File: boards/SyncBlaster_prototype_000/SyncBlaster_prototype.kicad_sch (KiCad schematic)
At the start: 19 parts, among them J1 DIN-5 MIDI IN, J2 TRS SYNC IN START/STOP, U1 4066, U2 ATtiny25-20P, U3 CNY17-3

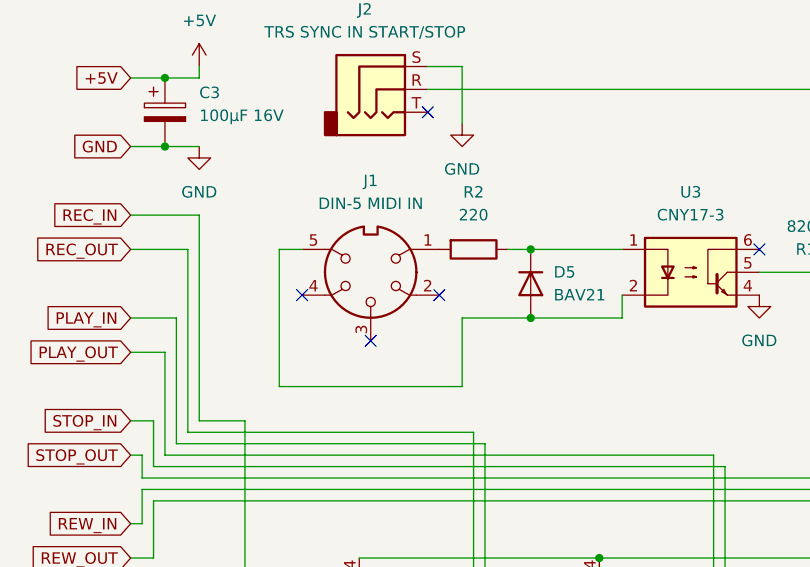
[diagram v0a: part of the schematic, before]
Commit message: prototype_000 board schematics release 3, MIDI OUT connection fix
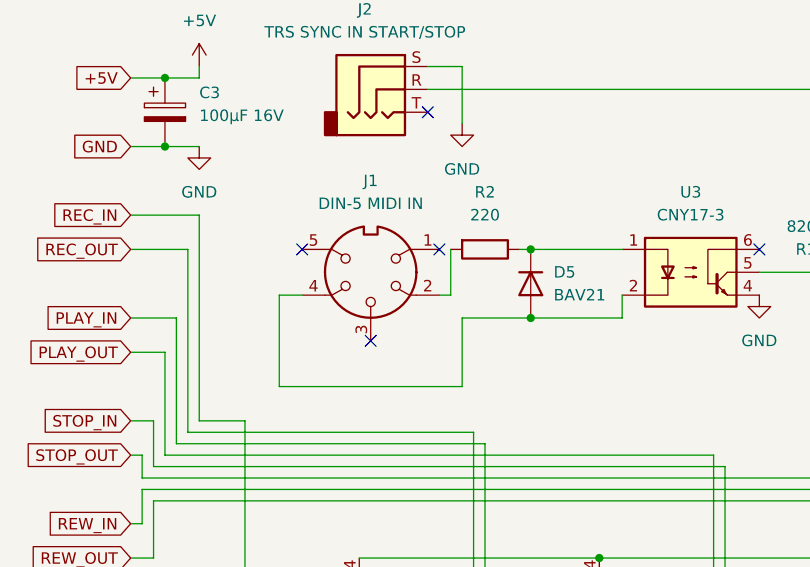
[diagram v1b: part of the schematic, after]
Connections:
- net at R2.2: now also J1.2; no longer J1.1
- net at J1.4: now also D5.2 (A), U3.2
- now unconnected: J1.5
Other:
- company: Copyright (c) Mateusz Maciejewski ^ TOXIC_DEATH.117, 2021 - 2023 -> Copyright (c) Mateusz Maciejewski ^ TOXIC_DEATH.117, 2021 - 2024
- moved on the sheet: R2
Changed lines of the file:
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@@
   (title_block
     (title "MIDI input interface for TASCAM DP00x")
-    (date "2023-06-16")
-    (rev "2")
-    (company "Copyright (c) Mateusz Maciejewski ^ TOXIC_DEATH.117, 2021 - 2023")
+    (date "2024-04-04")
+    (rev "3")
+    (company "Copyright (c) Mateusz Maciejewski ^ TOXIC_DEATH.117, 2021 - 2024")
   )
   (junction (at 93.98 107.95) (diameter 0) (color 0 0 0 0)
@@
   )
   (no_connect (at 119.38 107.95))
+  (no_connect (at 68.58 107.95))
   (no_connect (at 82.55 92.71))
-  (no_connect (at 68.58 113.03))
-  (no_connect (at 83.82 113.03))
+  (no_connect (at 83.82 107.95))
   (no_connect (at 76.2 118.11))
   (wire (pts (xy 176.53 157.48) (xy 154.94 157.48))
@@
     (stroke (width 0) (type default))
   )
-  (wire (pts (xy 66.04 107.95) (xy 68.58 107.95))
-    (stroke (width 0) (type default))
-  )
   (wire (pts (xy 49.53 115.57) (xy 54.61 115.57))
     (stroke (width 0) (type default))
@@
     (stroke (width 0) (type default))
   )
+  (wire (pts (xy 85.09 113.03) (xy 85.09 107.95))
+    (stroke (width 0) (type default))
+  )
   (wire (pts (xy 115.57 166.37) (xy 170.18 166.37))
     (stroke (width 0) (type default))
@@
     (stroke (width 0) (type default))
   )
+  (wire (pts (xy 66.04 113.03) (xy 68.58 113.03))
+    (stroke (width 0) (type default))
+  )
   (wire (pts (xy 134.62 110.49) (xy 134.62 91.44))
     (stroke (width 0) (type default))
@@
     (stroke (width 0) (type default))
   )
-  (wire (pts (xy 66.04 107.95) (xy 66.04 123.19))
+  (wire (pts (xy 66.04 113.03) (xy 66.04 123.19))
     (stroke (width 0) (type default))
   )
@@
     (stroke (width 0) (type default))
   )
-  (wire (pts (xy 91.44 107.95) (xy 93.98 107.95))
+  (wire (pts (xy 92.71 107.95) (xy 93.98 107.95))
     (stroke (width 0) (type default))
   )
@@
   )
   (wire (pts (xy 172.72 163.83) (xy 172.72 109.22))
+    (stroke (width 0) (type default))
+  )
+  (wire (pts (xy 85.09 113.03) (xy 83.82 113.03))
     (stroke (width 0) (type default))
   )
@@
     )
   )
-  (symbol (lib_id "Device:R") (at 87.63 107.95 270) (unit 1)
+  (symbol (lib_id "Device:R") (at 88.9 107.95 270) (unit 1)
     (in_bom yes) (on_board yes) (dnp no)
-    (property "Reference" "R2" (at 87.63 101.6 90)
-      (effects (font (size 1.27 1.27)))
-    )
-    (property "Value" "220" (at 87.63 104.14 90)
-      (effects (font (size 1.27 1.27)))
-    )
-    (property "Footprint" "" (at 87.63 106.172 90)
-      (effects (font (size 1.27 1.27)) hide)
-    )
-    (property "Datasheet" "~" (at 87.63 107.95 0)
-      (effects (font (size 1.27 1.27)) hide)
-    )
-    (pin "1")
-    (pin "2")
-    (instances
-      (project "SyncBlaster"
+    (property "Reference" "R2" (at 88.9 101.6 90)
+      (effects (font (size 1.27 1.27)))
+    )
+    (property "Value" "220" (at 88.9 104.14 90)
+      (effects (font (size 1.27 1.27)))
+    )
+    (property "Footprint" "" (at 88.9 106.172 90)
+      (effects (font (size 1.27 1.27)) hide)
+    )
+    (property "Datasheet" "~" (at 88.9 107.95 0)
+      (effects (font (size 1.27 1.27)) hide)
+    )
+    (pin "1")
+    (pin "2")
+    (instances
+      (project "SyncBlaster_prototype"
         (path "/32dfbc9d-88bc-4ac5-b7ea-f4ca99c6c011"
           (reference "R2") (unit 1)
@@
     (pin "5")
     (instances
-      (project "SyncBlaster"
+      (project "SyncBlaster_prototype"
         (path "/32dfbc9d-88bc-4ac5-b7ea-f4ca99c6c011"
           (reference "J1") (unit 1)
@@
     (pin "T")
     (instances
-      (project "SyncBlaster"
+      (project "SyncBlaster_prototype"
         (path "/32dfbc9d-88bc-4ac5-b7ea-f4ca99c6c011"
           (reference "J2") (unit 1)
@@
     (pin "12")
     (instances
-      (project "SyncBlaster"
+      (project "SyncBlaster_prototype"
         (path "/32dfbc9d-88bc-4ac5-b7ea-f4ca99c6c011"
           (reference "U1") (unit 2)
@@
     (pin "1")
     (instances
-      (project "SyncBlaster"
+      (project "SyncBlaster_prototype"
         (path "/32dfbc9d-88bc-4ac5-b7ea-f4ca99c6c011"
           (reference "#PWR06") (unit 1)
@@
     (pin "1")
     (instances
-      (project "SyncBlaster"
+      (project "SyncBlaster_prototype"
         (path "/32dfbc9d-88bc-4ac5-b7ea-f4ca99c6c011"
           (reference "#PWR010") (unit 1)
@@
     (pin "1")
     (instances
-      (project "SyncBlaster"
+      (project "SyncBlaster_prototype"
         (path "/32dfbc9d-88bc-4ac5-b7ea-f4ca99c6c011"
           (reference "#PWR09") (unit 1)
@@
     (pin "2")
     (instances
-      (project "SyncBlaster"
+      (project "SyncBlaster_prototype"
         (path "/32dfbc9d-88bc-4ac5-b7ea-f4ca99c6c011"
           (reference "D3") (unit 1)
@@
     (pin "2")
     (instances
-      (project "SyncBlaster"
+      (project "SyncBlaster_prototype"
         (path "/32dfbc9d-88bc-4ac5-b7ea-f4ca99c6c011"
           (reference "D4") (unit 1)
@@
     (pin "1")
     (instances
-      (project "SyncBlaster"
+      (project "SyncBlaster_prototype"
         (path "/32dfbc9d-88bc-4ac5-b7ea-f4ca99c6c011"
           (reference "#PWR03") (unit 1)
@@
     (pin "1")
     (instances
-      (project "SyncBlaster"
+      (project "SyncBlaster_prototype"
         (path "/32dfbc9d-88bc-4ac5-b7ea-f4ca99c6c011"
           (reference "#PWR08") (unit 1)
@@
     (pin "2")
     (instances
-      (project "SyncBlaster"
+      (project "SyncBlaster_prototype"
         (path "/32dfbc9d-88bc-4ac5-b7ea-f4ca99c6c011"
           (reference "R4") (unit 1)
@@
     (pin "1")
     (instances
-      (project "SyncBlaster"
+      (project "SyncBlaster_prototype"
         (path "/32dfbc9d-88bc-4ac5-b7ea-f4ca99c6c011"
           (reference "#PWR02") (unit 1)
@@
     (pin "2")
     (instances
-      (project "SyncBlaster"
+      (project "SyncBlaster_prototype"
         (path "/32dfbc9d-88bc-4ac5-b7ea-f4ca99c6c011"
           (reference "R3") (unit 1)
@@
     (pin "8")
     (instances
-      (project "SyncBlaster"
+      (project "SyncBlaster_prototype"
         (path "/32dfbc9d-88bc-4ac5-b7ea-f4ca99c6c011"
           (reference "U2") (unit 1)
@@
     (pin "2")
     (instances
-      (project "SyncBlaster"
+      (project "SyncBlaster_prototype"
         (path "/32dfbc9d-88bc-4ac5-b7ea-f4ca99c6c011"
           (reference "R1") (unit 1)
@@
     (pin "12")
     (instances
-      (project "SyncBlaster"
+      (project "SyncBlaster_prototype"
         (path "/32dfbc9d-88bc-4ac5-b7ea-f4ca99c6c011"
           (reference "U1") (unit 4)
@@
     (pin "6")
     (instances
-      (project "SyncBlaster"
+      (project "SyncBlaster_prototype"
         (path "/32dfbc9d-88bc-4ac5-b7ea-f4ca99c6c011"
           (reference "U3") (unit 1)
@@
     (pin "2")
     (instances
-      (project "SyncBlaster"
+      (project "SyncBlaster_prototype"
         (path "/32dfbc9d-88bc-4ac5-b7ea-f4ca99c6c011"
           (reference "R6") (unit 1)
@@
     (pin "12")
     (instances
-      (project "SyncBlaster"
+      (project "SyncBlaster_prototype"
         (path "/32dfbc9d-88bc-4ac5-b7ea-f4ca99c6c011"
           (reference "U1") (unit 1)
@@
     (pin "2")
     (instances
-      (project "SyncBlaster"
+      (project "SyncBlaster_prototype"
         (path "/32dfbc9d-88bc-4ac5-b7ea-f4ca99c6c011"
           (reference "C1") (unit 1)
@@
     (pin "1")
     (instances
-      (project "SyncBlaster"
+      (project "SyncBlaster_prototype"
         (path "/32dfbc9d-88bc-4ac5-b7ea-f4ca99c6c011"
           (reference "#PWR01") (unit 1)
@@
     (pin "2")
     (instances
-      (project "SyncBlaster"
+      (project "SyncBlaster_prototype"
         (path "/32dfbc9d-88bc-4ac5-b7ea-f4ca99c6c011"
           (reference "R5") (unit 1)
@@
     (pin "1")
     (instances
-      (project "SyncBlaster"
+      (project "SyncBlaster_prototype"
         (path "/32dfbc9d-88bc-4ac5-b7ea-f4ca99c6c011"
           (reference "#PWR05") (unit 1)
@@
     (pin "2")
     (instances
-      (project "SyncBlaster"
+      (project "SyncBlaster_prototype"
         (path "/32dfbc9d-88bc-4ac5-b7ea-f4ca99c6c011"
           (reference "C2") (unit 1)
@@
     (pin "2")
     (instances
-      (project "SyncBlaster"
+      (project "SyncBlaster_prototype"
         (path "/32dfbc9d-88bc-4ac5-b7ea-f4ca99c6c011"
           (reference "D5") (unit 1)
@@
     (pin "1")
     (instances
-      (project "SyncBlaster"
+      (project "SyncBlaster_prototype"
         (path "/32dfbc9d-88bc-4ac5-b7ea-f4ca99c6c011"
           (reference "#PWR04") (unit 1)
@@
     (pin "2")
     (instances
-      (project "SyncBlaster"
+      (project "SyncBlaster_prototype"
         (path "/32dfbc9d-88bc-4ac5-b7ea-f4ca99c6c011"
           (reference "C3") (unit 1)
@@
     (pin "1")
     (instances
-      (project "SyncBlaster"
+      (project "SyncBlaster_prototype"
         (path "/32dfbc9d-88bc-4ac5-b7ea-f4ca99c6c011"
           (reference "#PWR07") (unit 1)
@@
     (pin "2")
     (instances
-      (project "SyncBlaster"
+      (project "SyncBlaster_prototype"
         (path "/32dfbc9d-88bc-4ac5-b7ea-f4ca99c6c011"
           (reference "D2") (unit 1)
@@
     (pin "2")
     (instances
-      (project "SyncBlaster"
+      (project "SyncBlaster_prototype"
         (path "/32dfbc9d-88bc-4ac5-b7ea-f4ca99c6c011"
           (reference "D1") (unit 1)
@@
     (pin "12")
     (instances
-      (project "SyncBlaster"
+      (project "SyncBlaster_prototype"
         (path "/32dfbc9d-88bc-4ac5-b7ea-f4ca99c6c011"
           (reference "U1") (unit 3)
